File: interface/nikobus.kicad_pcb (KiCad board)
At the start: 2 copper layers, 70 x 88 mm, 28 parts, among them J1 Conn_01x06, J2 DB9_Female, P2 Bus, Q1 BC547, Q2 BC547, Q3 BC547, Q4 BC547, U1 PIC16F690, U3 TLC274

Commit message: Almost finished PCB design
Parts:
- removed P2: Bus, Connectors:PINHEAD1-2
- added C2: 330uF, Capacitors_THT:CP_Radial_D10.0mm_P5.00mm, F.Cu at (102.9, 62.2)
- added C3: 0.33uF, Capacitors_THT:C_Disc_D3.4mm_W2.1mm_P2.50mm, F.Cu at (111.8, 61.0)
- added C5: 0,1uF, Capacitors_THT:C_Disc_D3.4mm_W2.1mm_P2.50mm, F.Cu at (120.7, 90.2)
- added D1: 1N4148, Diodes_THT:D_DO-35_SOD27_P10.16mm_Horizontal, F.Cu at (109.2, 113.0)
- added D3: 6V8, Diodes_THT:D_DO-35_SOD27_P10.16mm_Horizontal, F.Cu at (124.5, 99.1)
- added J3: 12V, Pin_Headers:Pin_Header_Straight_1x02_Pitch2.54mm, F.Cu at (116.6, 54.6)
- added J4: BUS, Pin_Headers:Pin_Header_Straight_1x02_Pitch2.54mm, F.Cu at (125.7, 119.4)
- added R13: 330, Resistors_THT:R_Axial_DIN0207_L6.3mm_D2.5mm_P10.16mm_Horizontal, F.Cu at (113.0, 88.9)
- added U2: 78L05, TO_SOT_Packages_THT:TO-92_Inline_Narrow_Oval, F.Cu at (116.8, 63.5)
- C4: value 0,1uF -> 0.1uF
- D2: value 1N4148 -> D_Bridge_+AA-; footprint Diodes_THT:D_DO-35_SOD27_P7.62mm_Horizontal -> Diodes_THT:Diode_Bridge_DIP-4_W7.62mm_P5.08mm
- D4: value 6V8 -> 2V7; footprint Diodes_THT:D_DO-35_SOD27_P7.62mm_Horizontal -> Diodes_THT:D_DO-35_SOD27_P10.16mm_Horizontal
- D5: value 2V7 -> LED; footprint Diodes_THT:D_DO-35_SOD27_P7.62mm_Horizontal -> LEDs:LED_D3.0mm_Horizontal_O3.81mm_Z2.0mm
- D6, D7: footprint Diodes_THT:D_DO-35_SOD27_P7.62mm_Horizontal -> Diodes_THT:D_DO-35_SOD27_P10.16mm_Horizontal
- J1: value Conn_01x06 -> Programmer
- J2: value DB9_Female -> RS232; footprint Pin_Headers:Pin_Header_Straight_1x09_Pitch2.54mm -> Pin_Headers:Pin_Header_Straight_1x03_Pitch2.54mm
- R1, R10, R11, R12, R2, R3, R4, R5, R6, R7, R8, R9: footprint Resistors_THT:R_Axial_DIN0204_L3.6mm_D1.6mm_P7.62mm_Horizontal -> Resistors_THT:R_Axial_DIN0207_L6.3mm_D2.5mm_P10.16mm_Horizontal
- U3: value TLC274 -> LM358; footprint Housings_DIP:DIP-14_W7.62mm -> Housings_DIP:DIP-8_W7.62mm
- moved D5 150.1 mm to (111.8, 44.5)
- moved C4 139.8 mm to (121.9, 63.5), turned to 90 degrees
- moved D7 134.0 mm to (109.2, 78.7), turned to 270 degrees
- moved U3 130.7 mm to (125.7, 86.4), turned to 180 degrees
- moved Q2 125.1 mm to (100.3, 113.0)
- moved R11 122.0 mm to (121.9, 67.3), turned to 180 degrees
- moved R6 120.0 mm to (101.6, 99.1)
- moved R5 120.0 mm to (101.6, 95.2)
- moved R10 119.6 mm to (139.7, 120.7)
- moved U1 118.7 mm to (87.6, 80.0)
- moved C1 118.7 mm to (90.2, 76.2)
- moved Q4 117.6 mm to (118.1, 104.1)
- moved Q3 117.4 mm to (118.1, 97.8), turned to 90 degrees
- moved R9 117.3 mm to (129.5, 115.6)
- moved R8 114.3 mm to (134.6, 106.7)
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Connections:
- C1 pad 1: (no net) -> VDD
- C1 pad 2: (no net) -> GND
- C4 pad 1: (no net) -> VDD
- C4 pad 2: (no net) -> GND
- D2 pad 1: (no net) -> Net-(C2-Pad1)
- D2 pad 2: Net-(D2-Pad2) -> GND
- D4 pad 1: Net-(D4-Pad1) -> Net-(D3-Pad1)
- D4 pad 2: (no net) -> Net-(D4-Pad2)
- D5 pad 2: (no net) -> VDD
- D6 pad 1: (no net) -> Net-(D6-Pad1)
- D6 pad 2: Net-(D6-Pad2) -> GND
- D7 pad 1: (no net) -> Net-(D7-Pad1)
- D7 pad 2: Net-(D7-Pad2) -> GND
- J1 pad 2: (no net) -> VDD
- J1 pad 3: (no net) -> GND
- J2 pad 1: (no net) -> GND
- Q1 pad 1: Net-(J2-Pad2) -> Net-(J2-Pad3)
- Q1 pad 3: (no net) -> GND
- Q2 pad 2: Net-(D2-Pad2) -> Net-(D1-Pad1)
- Q2 pad 3: (no net) -> GND
- Q3 pad 3: (no net) -> GND
- Q4 pad 3: (no net) -> GND
- R10 pad 2: (no net) -> GND
- R11 pad 1: (no net) -> Net-(D5-Pad1)
- R11 pad 2: Net-(D6-Pad2) -> GND
- R12 pad 1: (no net) -> VDD
- R12 pad 2: Net-(D7-Pad2) -> Net-(D6-Pad1)
- R2 pad 1: Net-(J2-Pad2) -> Net-(J2-Pad3)
- R2 pad 2: (no net) -> VDD
- R3 pad 1: Net-(J2-Pad3) -> Net-(J2-Pad2)
- R3 pad 2: Net-(D2-Pad2) -> Net-(D1-Pad1)
- R4 pad 2: (no net) -> VDD
- R7 pad 1: Net-(D4-Pad1) -> Net-(D3-Pad2)
- R8 pad 1: Net-(D5-Pad1) -> Net-(D4-Pad2)
- R9 pad 1: (no net) -> Net-(D3-Pad1)
- U1 pad 1: (no net) -> VDD
- U1 pad 20: (no net) -> GND
- U3 pad 3: Net-(D6-Pad2) -> Net-(D6-Pad1)
- U3 pad 4: (no net) -> GND
- U3 pad 5: Net-(D7-Pad2) -> Net-(D7-Pad1)
- U3 pad 8: Net-(U3-Pad10) -> VDD
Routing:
- net VDD: track 0.00 -> 155.6 mm
- net Net-(R10-Pad1): track 0.00 -> 51.6 mm
- net Net-(U1-Pad15): track 0.00 -> 36.1 mm
- net Net-(J1-Pad1): track 0.00 -> 29.9 mm
- net Net-(J2-Pad3): track 0.00 -> 29.8 mm
- net Net-(Q2-Pad1): track 0.00 -> 29.6 mm
- net Net-(U1-Pad16): track 0.00 -> 25.5 mm
- net Net-(D3-Pad1): track 0.00 -> 23.7 mm
- net Net-(C2-Pad1): track 0.00 -> 18.7 mm
- net Net-(J2-Pad2): track 0.00 -> 16.3 mm
- net Net-(D6-Pad1): track 0.00 -> 13.5 mm
- net Net-(D2-Pad4): track 0.00 -> 13.4 mm
- net Net-(Q1-Pad2): track 0.00 -> 12.5 mm
- net Net-(R1-Pad1): track 0.00 -> 11.7 mm
- net Net-(D1-Pad1): track 0.00 -> 9.42 mm
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- added copper zone on F.Cu, net (none)
- added copper zone on B.Cu, net GND
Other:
- net class Power added: clearance 0.4, trace_width 1, via_dia 0.6, via_drill 0.4
- net class Signal added: clearance 0.2, trace_width 0.25, via_dia 0.6, via_drill 0.4
- board text added: "12V"
- board text added: "Bus"
- board text added: "Clk"
- board text added: "Data"
- board text added: "Gnd"
- board text added: "Mclr"
- board text added: "Nc"
- board text added: "Power"
- board text added: "RS232"
- board text added: "Rx"
- board text added: "Tx"
- board text added: "Vdd"

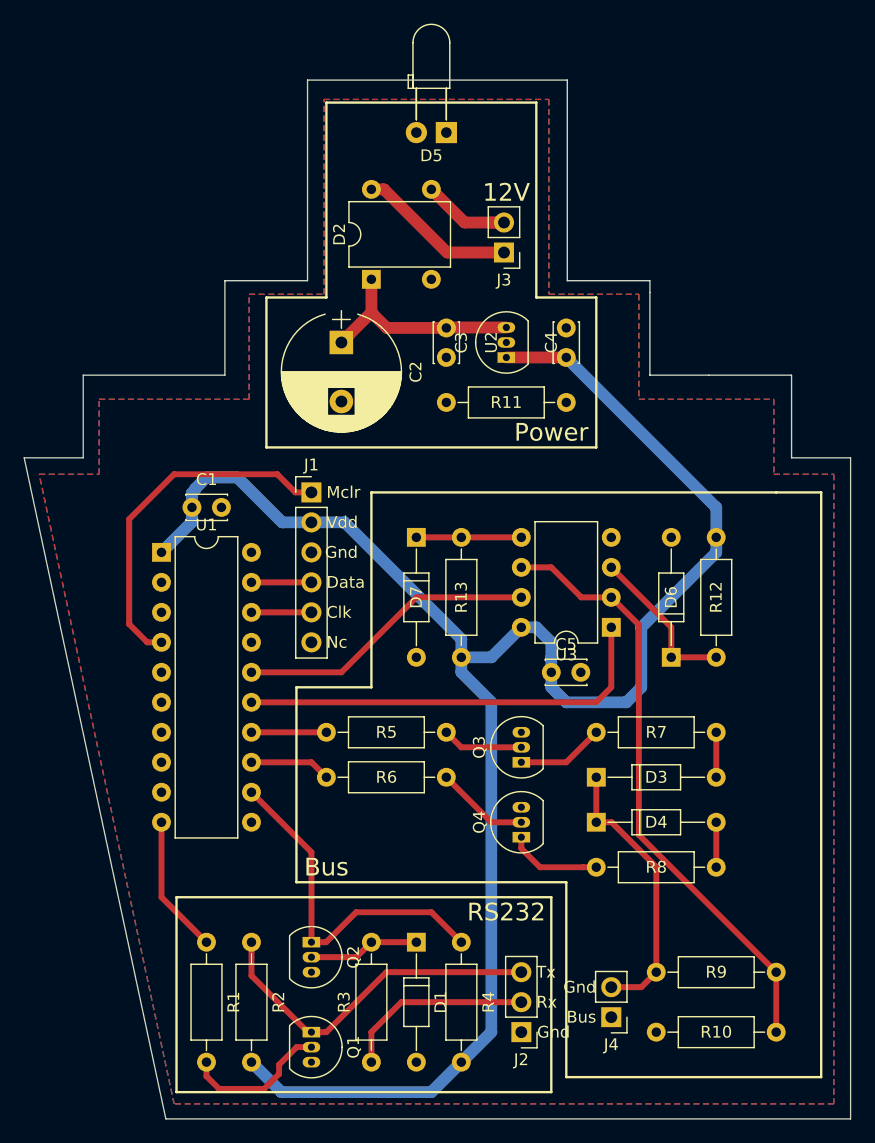
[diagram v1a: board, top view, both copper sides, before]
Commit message: Add 78l05 protection diode and increased pad sizes
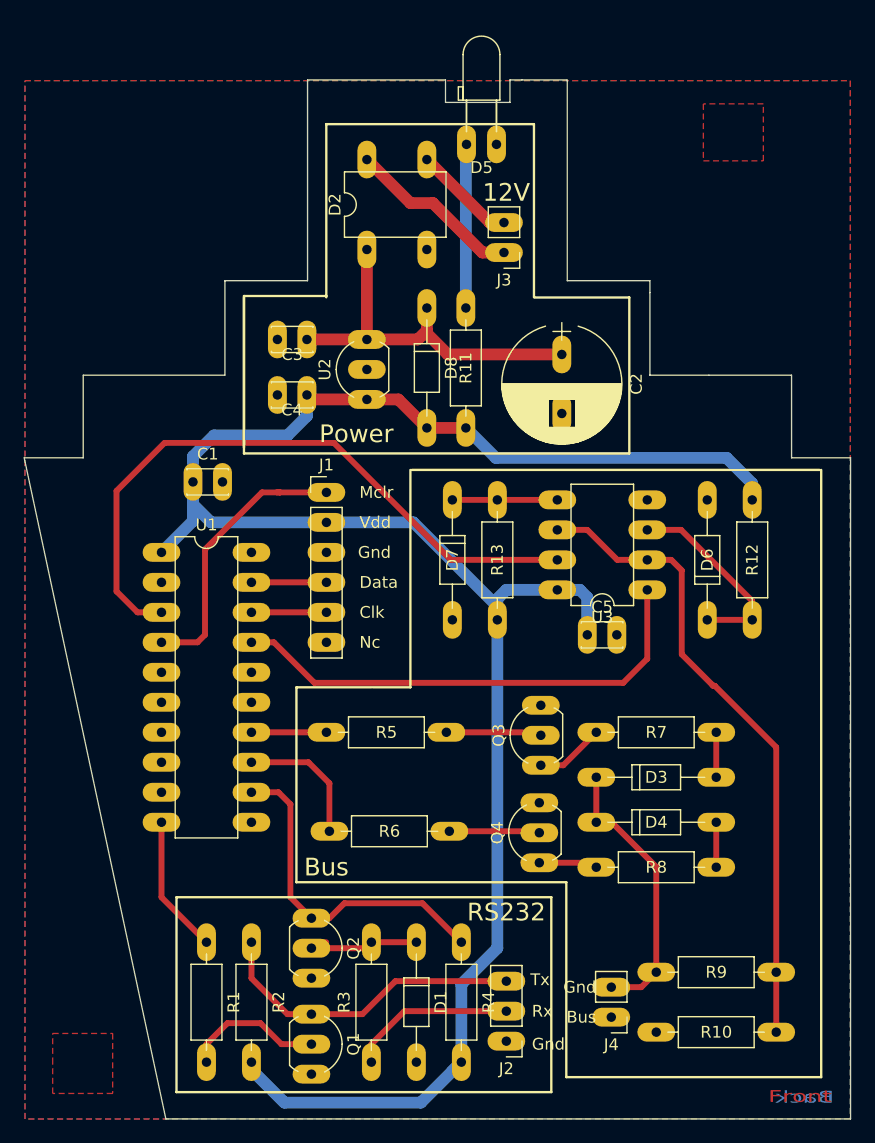
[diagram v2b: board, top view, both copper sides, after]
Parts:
- added D8: 1N4148, Diodes_THT:D_DO-35_SOD27_P10.16mm_Horizontal, F.Cu at (110.1, 59.3)
- Q1, Q2, Q3, Q4, U2: footprint TO_SOT_Packages_THT:TO-92_Inline_Narrow_Oval -> TO_SOT_Packages_THT:TO-92_Inline_Wide
- moved C4 22.2 mm to (99.9, 66.7), turned to 180 degrees
- moved C2 18.7 mm to (121.5, 63.2)
- moved U2 12.3 mm to (105.0, 67.1)
- moved C3 11.9 mm to (99.9, 62.0), turned to 180 degrees
- moved R11 8.78 mm to (113.4, 69.5), turned to 90 degrees
- moved R6 4.58 mm to (101.9, 103.6)
- moved D6 4.40 mm to (133.9, 85.7)
- moved R13 4.40 mm to (116.1, 85.7)
- moved D7 4.40 mm to (112.3, 75.6)
- moved R12 4.40 mm to (137.7, 75.6)
- moved C5 4.40 mm to (123.7, 87.0)
- moved U3 4.40 mm to (128.8, 83.2)
- moved D5 4.36 mm to (116.0, 45.5)
- moved Q4 2.64 mm to (119.6, 106.3)
- moved D2 2.55 mm to (105.0, 54.4)
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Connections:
- D5 pad 1: Net-(D5-Pad1) -> GND
- D5 pad 2: VDD -> Net-(D5-Pad2)
- R11 pad 1: Net-(D5-Pad1) -> VDD
- R11 pad 2: GND -> Net-(D5-Pad2)
- U1 pad 15: Net-(U1-Pad15) -> (no net)
- U1 pad 16: Net-(U1-Pad16) -> (no net)
- U1 pad 17: (no net) -> Net-(U1-Pad17)
- U1 pad 3: (no net) -> Net-(U1-Pad3)
- U3 pad 1: Net-(U1-Pad15) -> Net-(U1-Pad17)
- U3 pad 7: Net-(U1-Pad16) -> Net-(U1-Pad3)
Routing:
- net Net-(U1-Pad3): track 0.00 -> 56.2 mm
- net Net-(U1-Pad17): track 0.00 -> 41.6 mm
- net Net-(U1-Pad15): track 36.1 -> 0.00 mm
- net Net-(U1-Pad16): track 25.5 -> 0.00 mm
- net VDD: track 155.6 -> 172.3 mm
- net Net-(D5-Pad2): track 0.00 -> 13.9 mm
- net Net-(C2-Pad1): track 18.7 -> 32.4 mm
- net Net-(R10-Pad1): track 51.6 -> 56.6 mm
- net Net-(J1-Pad1): track 29.9 -> 24.9 mm
- net Net-(R6-Pad1): track 6.88 -> 11.4 mm
- net Net-(D6-Pad1): track 13.5 -> 16.8 mm
- net Net-(Q4-Pad1): track 7.96 -> 4.98 mm
- net Net-(J2-Pad3): track 29.8 -> 27.8 mm
- net Net-(Q4-Pad2): track 7.93 -> 6.22 mm
- net Net-(Q3-Pad1): track 7.40 -> 5.86 mm
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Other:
- outline, holes or cut-outs redrawn
- net class Default: clearance 0.2 -> 0.3; trace_width 0.25 -> 0.5
- net class Signal removed
- rule trace_clearance: 0.2 -> 0.3
- rule trace_min: 0.2 -> 0.5
- board text added: "Back"
- board text added: "Front"

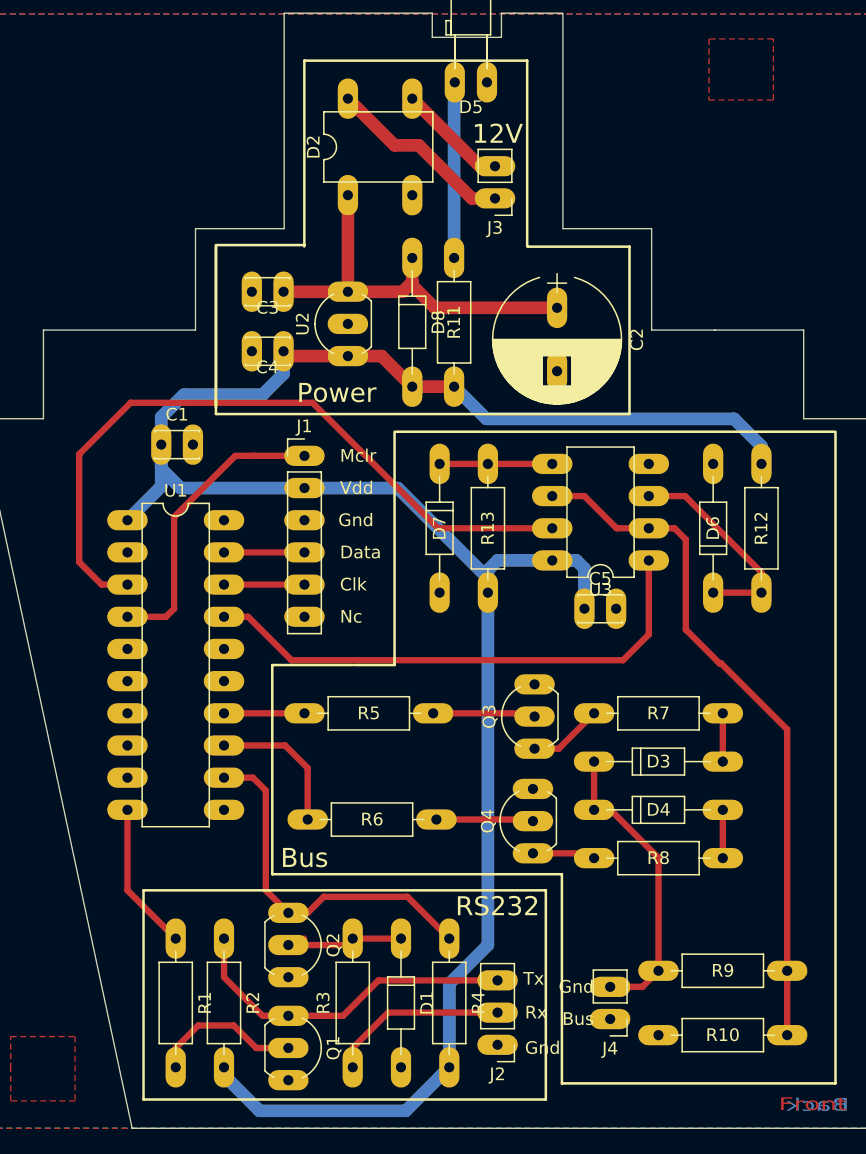
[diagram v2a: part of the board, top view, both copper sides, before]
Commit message: Swap front and back layer
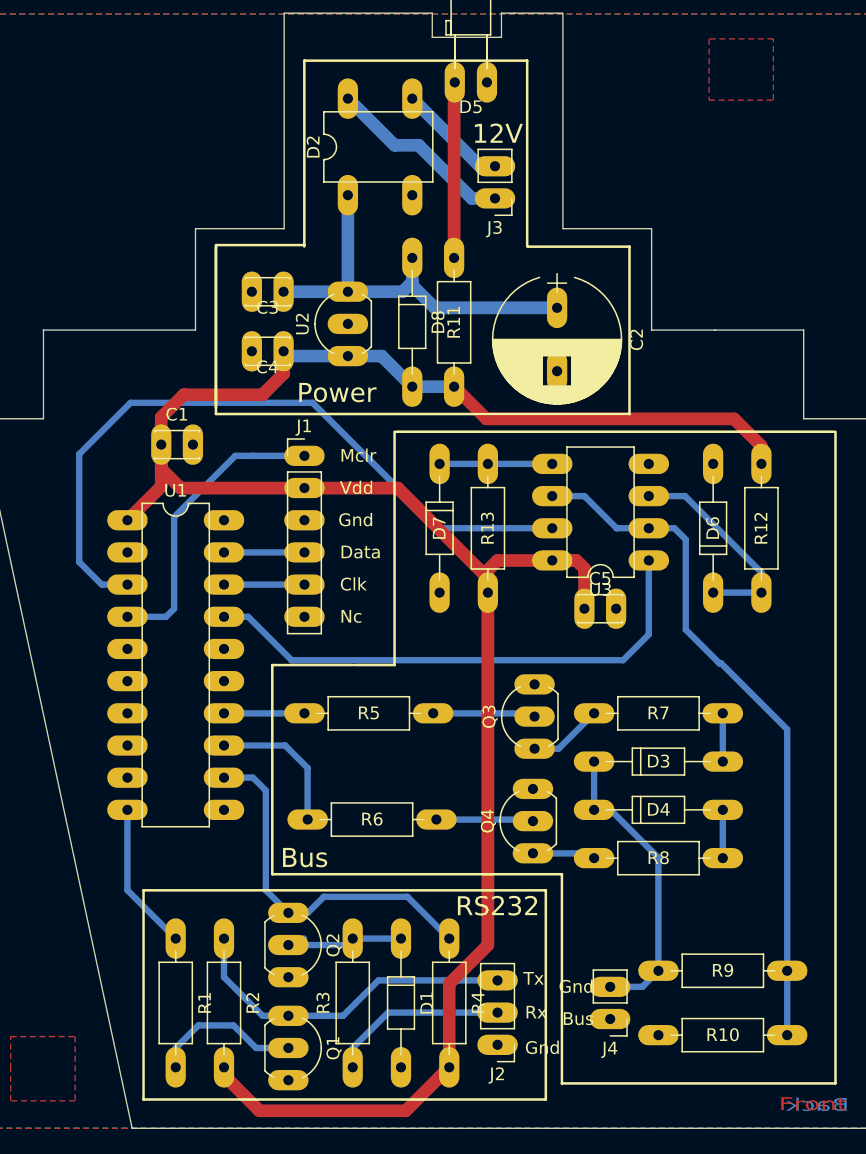
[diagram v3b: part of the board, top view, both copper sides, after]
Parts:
- D7: value 2V7 -> 3V3

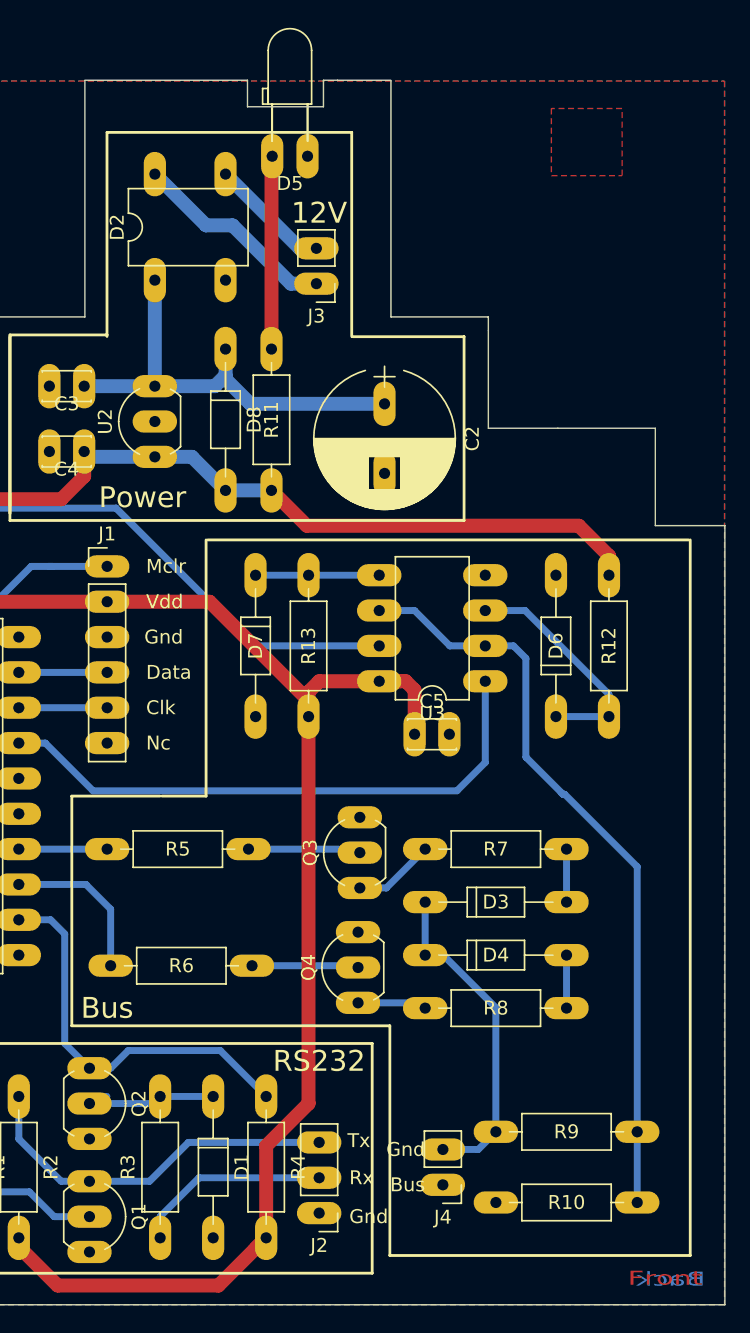
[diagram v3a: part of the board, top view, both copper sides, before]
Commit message: Add tvs zener location to the board
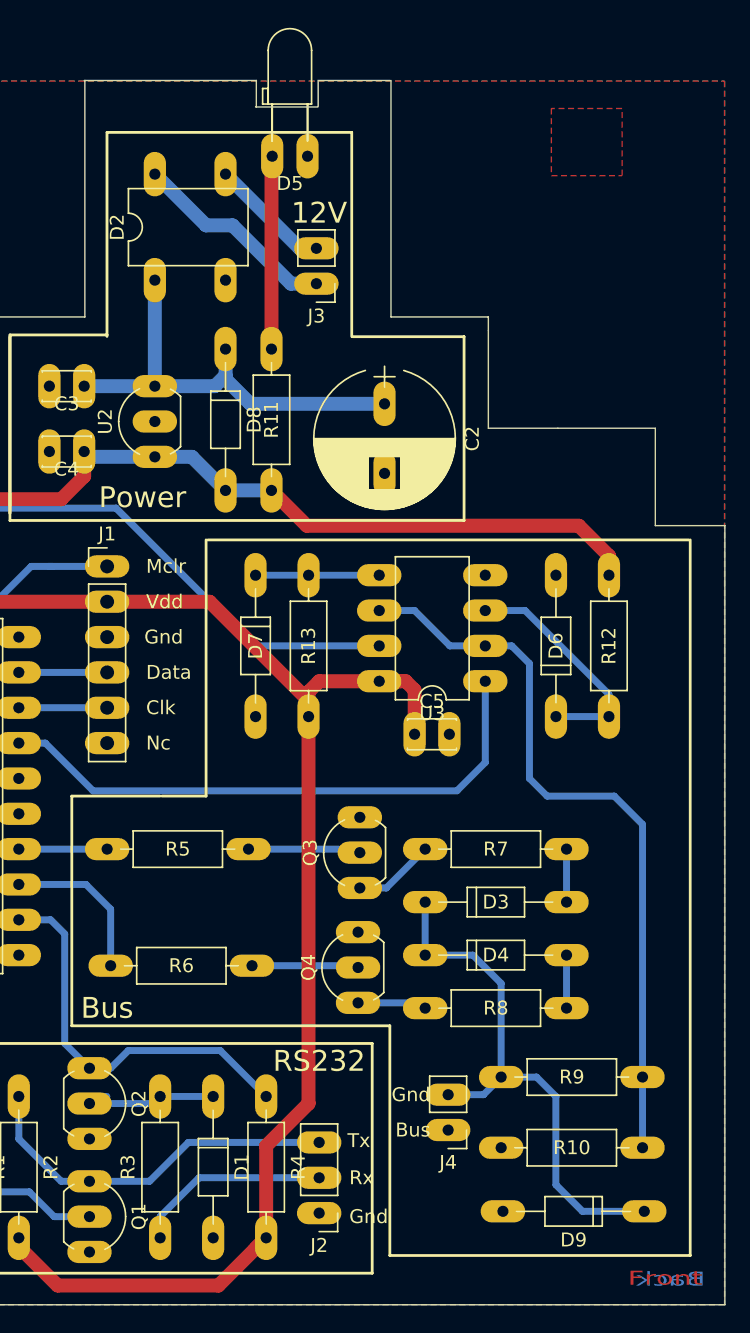
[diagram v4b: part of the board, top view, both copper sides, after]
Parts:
- added D9: D_TVS, Diodes_THT:D_DO-35_SOD27_P10.16mm_Horizontal, F.Cu at (140.2, 121.3)
- moved R10 3.96 mm to (140.1, 116.7)
- moved J4 3.96 mm to (126.1, 115.4)
- moved R9 3.96 mm to (129.9, 111.6)
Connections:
- J1 pad 6: (no net) -> Net-(J1-Pad6)
- U1 pad 11: (no net) -> Net-(U1-Pad11)
- U1 pad 15: (no net) -> Net-(U1-Pad15)
- U1 pad 16: (no net) -> Net-(U1-Pad16)
- U1 pad 2: (no net) -> Net-(U1-Pad2)
- U1 pad 5: (no net) -> Net-(U1-Pad5)
- U1 pad 6: (no net) -> Net-(U1-Pad6)
- U1 pad 7: (no net) -> Net-(U1-Pad7)
- U1 pad 8: (no net) -> Net-(U1-Pad8)
- U1 pad 9: (no net) -> Net-(U1-Pad9)
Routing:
- net Net-(D3-Pad1): track 23.7 -> 40.5 mm
- net Net-(R10-Pad1): track 56.6 -> 54.8 mm
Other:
- outline, holes or cut-outs redrawn
